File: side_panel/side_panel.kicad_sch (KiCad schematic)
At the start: 37 parts, among them CN4 DLL-5569-6AW, CN5 KF2EDGRC-5.08-4P, SW15 KH-6X6X6H-STM, SW16 KH-6X6X6H-STM, U19 PY32F030K28U6TR, U20 WAFER-XH254WZ-2A, U21 WAFER-XH254WZ-2A, U22 WAFER-XH254WZ-4A, U23 KF128-5.08-2P, U24 KF128-5.08-2P, X3 AFA01-S05FCA-00, X4 AFA01-S05FCA-00

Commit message: feat: 添加侧电机板基础元件布局
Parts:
- removed TP14, TP15, TP16, TP17: 1.0mm, PCM_SparkFun-Connector:TestPoint-1.0mm, symbol PCM_SparkFun-Connector:TestPoint_1.0mm
- removed X4: AFA01-S05FCA-00, lcsc_footprints:C262753_FPC-SMD_AFA01-S05FCA-00, symbol lcsc_imported:AFA01-S05FCA-00
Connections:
- net TOF/XSHUT is gone; now on net TOF_XSHUT: X3.1
- net TOF_SCL is gone; now on net RS485_PY32/RS485_RX: U19.21 (PA11)
- net TOF_SDA is gone; now on net RS485_PY32/RS485_DE: U19.22 (PA12)
- net 步进驱动/DIAG is gone; now on net MOTOR_ENC_A: U19.14 (PB0)
- net 步进驱动/DIR is gone; now on net PUSH_BUTTON_1: U19.5 (PF3)
- net 步进驱动/EN is gone; now on net EXT_ENC_B: U19.2 (OSCIN-PF0)
- net 步进驱动/UART_TX/RX is gone; now on net EXT_ENC_A: U19.3 (OSCOUT-PF1)
- net EXT_ENC_A: no longer U19.18 (PA8)
- net EXT_ENC_B: no longer U19.19 (PA9-OSC32OUT)
- net MOTOR_BI: now also U19.18 (PA8); no longer U19.10 (PA4)
- net MOTOR_ENC_A: no longer U19.27 (PB4)
- net MOTOR_ENC_B: now also U19.13 (PA7); no longer U19.28 (PB5)
- net MOTOR_FI: now also U19.17 (PB2); no longer U19.13 (PA7)
- net PUSH_BUTTON_1: no longer U19.9 (PA3)
- net PUSH_BUTTON_2: now also U19.7 (PA1); no longer U19.20 (PA10-OSC32IN)
- net RS485_PY32/RS485_DE: no longer U19.17 (PB2)
- net RS485_PY32/RS485_RX: no longer U19.30 (PB7)
- net RS485_PY32/RS485_TX: now also U19.20 (PA10-OSC32IN); no longer U19.29 (PB6)
- net TMC_STEP: now also U19.30 (PB7); no longer U19.12 (PA6)
- net TOF_XSHUT: now also U19.10 (PA4); no longer U19.7 (PA1)
- net 步进驱动/INDEX: no longer U19.8 (PA2)
- net SCL: now reaches U19.11 (PA5)
- net TMC_DIAG: now reaches U19.26 (PB3)
- new net SDA: U19.12 (PA6)
- new net TMC_DIR: U19.29 (PB6)
- new net TMC_EN: U19.28 (PB5)
- new net TMC_UART: U19.27 (PB4)
- no-connect marks 4 -> 8
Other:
- moved on the sheet: C50, CN4, CN5, R45, R47, R50, U21

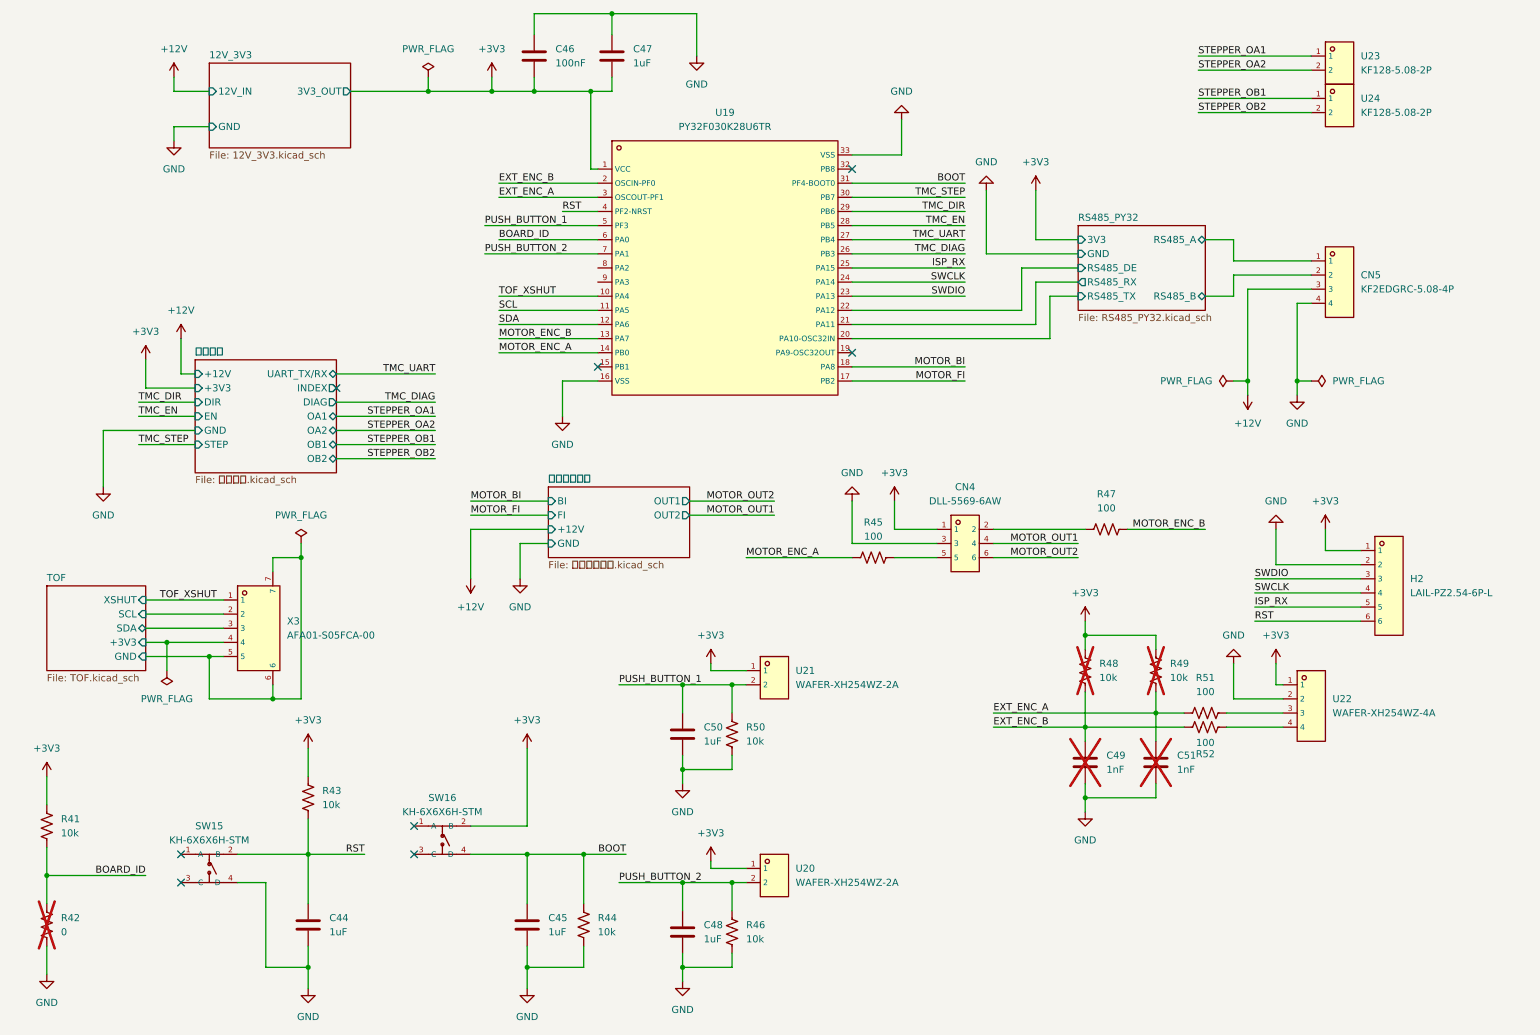
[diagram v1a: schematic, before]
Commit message: update: 更新侧板原理图，进行分类
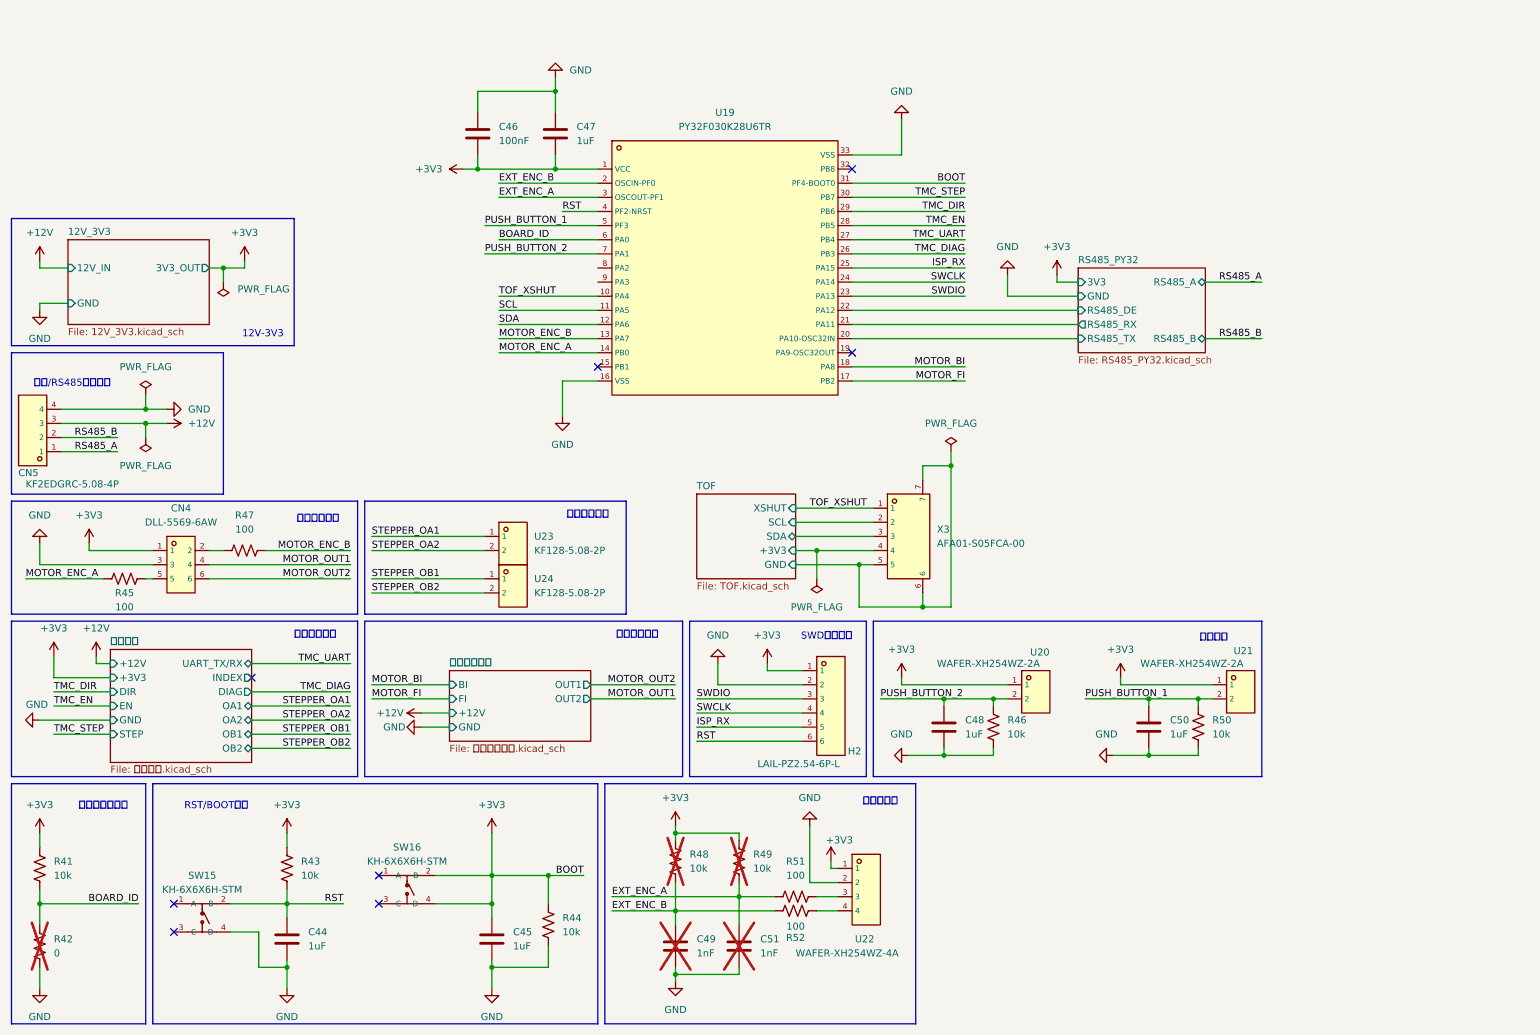
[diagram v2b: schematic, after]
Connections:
- net BOOT is gone; now on net +3V3: C45.1, R44.1, SW16.4 (D), U19.31 (PF4-BOOT0)
- net RS485_PY32/RS485_A renamed RS485_A
- net RS485_PY32/RS485_B renamed RS485_B
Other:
- note added: "12V-3V3"
- note added: "RST/BOOT电路"
- note added: "SWD烧录端口"
- note added: "升降电机驱动"
- note added: "外部按钮"
- note added: "外部编码器"
- note added: "左右板识别电阻"
- note added: "步进电机接口"
- note added: "步进电机驱动"
- note added: "电机输出接口"
- note added: "电源/RS485输入接口"
- moved on the sheet: C44, C45, C46, C47, C48, C49, C50, C51, CN4, H2, R41, R42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

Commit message: 更新针脚变动
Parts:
- added D1, D2: LED, LED_SMD:LED_0603_1608Metric, symbol Device:LED
- added R13: 10k, Resistor_SMD:R_0603_1608Metric, symbol PCM_SparkFun-Resistor:R
- added R14, R15: 1k, Resistor_SMD:R_0603_1608Metric, symbol PCM_SparkFun-Resistor:R
- C1: renamed from C44; value 1uF -> 100nF
- C3: renamed from C45; value 1uF -> 100nF
- R1: renamed from R41; footprint PCM_SparkFun-Resistor:R_0603_1608Metric -> Resistor_SMD:R_0603_1608Metric
- R10: renamed from R52; footprint PCM_SparkFun-Resistor:R_0603_1608Metric -> Resistor_SMD:R_0603_1608Metric
- R11: renamed from R46; footprint PCM_SparkFun-Resistor:R_0603_1608Metric -> Resistor_SMD:R_0603_1608Metric
- R12: renamed from R50; footprint PCM_SparkFun-Resistor:R_0603_1608Metric -> Resistor_SMD:R_0603_1608Metric
- R2: renamed from R42; footprint PCM_SparkFun-Resistor:R_0603_1608Metric -> Resistor_SMD:R_0603_1608Metric
- R3: renamed from R45; footprint PCM_SparkFun-Resistor:R_0603_1608Metric -> Resistor_SMD:R_0603_1608Metric
- R4: renamed from R47; footprint PCM_SparkFun-Resistor:R_0603_1608Metric -> Resistor_SMD:R_0603_1608Metric
- R5: renamed from R43; footprint PCM_SparkFun-Resistor:R_0603_1608Metric -> Resistor_SMD:R_0603_1608Metric
- R6: renamed from R44; footprint PCM_SparkFun-Resistor:R_0603_1608Metric -> Resistor_SMD:R_0603_1608Metric
- R7: renamed from R48; footprint PCM_SparkFun-Resistor:R_0603_1608Metric -> Resistor_SMD:R_0603_1608Metric
- R8: renamed from R49; footprint PCM_SparkFun-Resistor:R_0603_1608Metric -> Resistor_SMD:R_0603_1608Metric
- R9: renamed from R51; footprint PCM_SparkFun-Resistor:R_0603_1608Metric -> Resistor_SMD:R_0603_1608Metric
- renumbered C46 to C2, C47 to C4, C49 to C5, C51 to C6, C48 to C7, C50 to C8, CN5 to CN1, CN4 to CN2, H2 to H1, SW15 to SW1, SW16 to SW2, U23 to U1, U24 to U2, U19 to U3, U22 to U4, U20 to U5, U21 to U6, X3 to X1
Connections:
- net TOF/+3V3 is gone; now on net +3V3: X1.4
- net TOF/SCL is gone; now on net SCL: X1.2
- net TOF/SDA is gone; now on net SDA: X1.3
- net +12V: now also D1.2 (A)
- net +3V3: now also D2.2 (A); no longer C3.1, R6.1, SW2.4 (D), U3.31 (PF4-BOOT0)
- net GND: now also X1.5, R13.2, R15.2
- removed net TOF/GND: X1.5, X1.6, X1.7
- new net: R14.2, R15.1
- new net: D2.1 (K), R14.1
- new net: D1.1 (K), R13.1
- new net BOOT: C3.1, R6.1, SW2.4 (D), U3.31 (PF4-BOOT0)
- no-connect marks 8 -> 12
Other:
- note added: "TOF"
- note added: "电源指示灯"
- moved on the sheet: C3, R6, X1

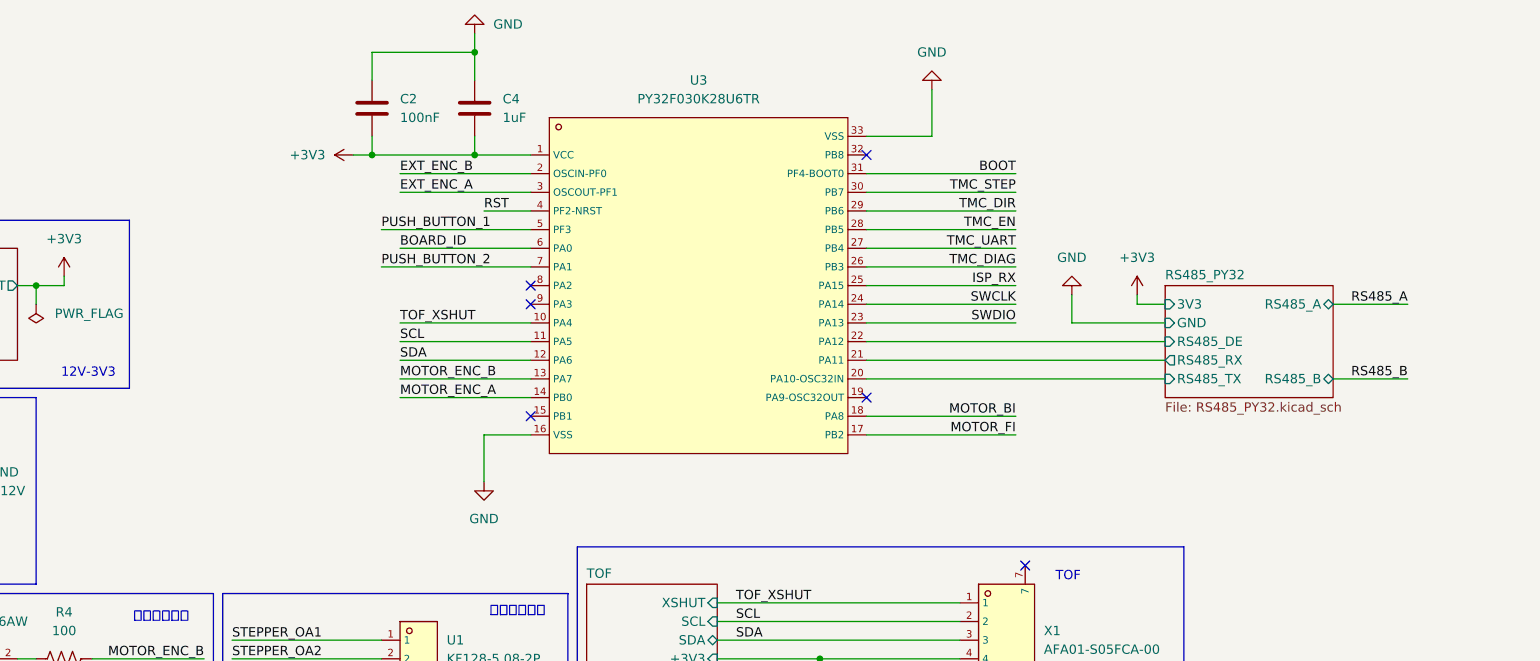
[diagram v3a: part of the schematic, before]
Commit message: update: 更新按钮小板设计，导出gerber文件
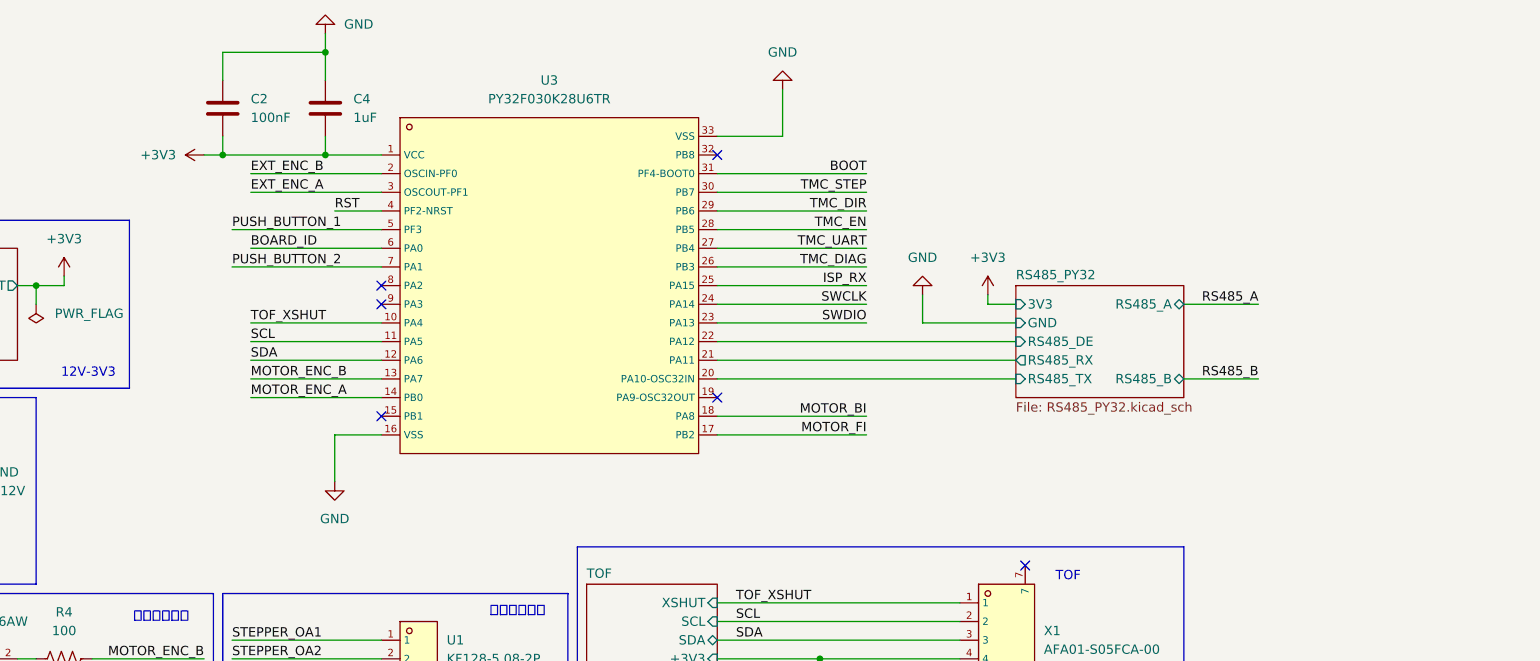
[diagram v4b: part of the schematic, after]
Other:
- moved on the sheet: C2, C4, U3
